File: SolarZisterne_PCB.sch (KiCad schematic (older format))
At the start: 4 parts

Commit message: Konzept auf I2C
Alle Temp und Strom Senoren werden über I2C angesteuert Digitale I/O werden auch über I2C erweiter. Kein AT MEGA mehr.
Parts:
- removed C? (x2): 22pF, symbol C
- removed U?: ATMEGA328P-PU, DIL28, symbol ATMEGA328P-PU
- removed Y?: Crystal 8MHz, symbol Crystal
- added JP?: Jumper_NO_Small, symbol Jumper_NO_Small
- added U?: WeMos_mini, symbol WeMos_mini
- added U?: MCP23008, symbol MCP23008
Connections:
- net labels removed: GND
- wire segments 15 -> 4
- no-connect marks 0 -> 4
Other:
- note added: "Pins D5, D6, D7, D8 werden durch SD Karte beansprucht\nPins D2, D1 werden für I2C Sensoren benutzt\nweitere 3 Pins für MCP73871 Solar Charger\nweitere 2 Pins für Ultraschallsensor"
- note added: "SDA\nSCL"
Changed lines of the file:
@@
 LIBS:contrib
 LIBS:valves
+LIBS:ESP8266
+LIBS:wemos_mini
+LIBS:SolarZisterne_PCB-cache
 EELAYER 25 0
 EELAYER END
@@
 $EndDescr
 $Comp
-L ATMEGA328P-PU U?
-U 1 1 5929E6B8
-P 3600 2600
-F 0 "U?" H 2850 3850 50  0000 L BNN
-F 1 "ATMEGA328P-PU" H 4000 1200 50  0000 L BNN
-F 2 "DIL28" H 3600 2600 50  0001 C CIN
-F 3 "" H 3600 2600 50  0001 C CNN
-	1    3600 2600
+L WeMos_mini U?
+U 1 1 59516611
+P 9250 1800
+F 0 "U?" H 9250 2300 60  0000 C CNN
+F 1 "WeMos_mini" H 9250 1300 60  0000 C CNN
+F 2 "" H 9800 1100 60  0000 C CNN
+F 3 "" H 9800 1100 60  0000 C CNN
+	1    9250 1800
 	1    0    0    -1
 $EndComp
+Text Notes 8250 950  0    60   ~ 0
+Pins D5, D6, D7, D8 werden durch SD Karte beansprucht\nPins D2, D1 werden für I2C Sensoren benutzt\nweitere 3 Pins für MCP73871 Solar Charger\nweitere 2 Pins für Ultraschallsensor
+NoConn ~ 9750 1850
+NoConn ~ 9750 1750
+NoConn ~ 9750 1650
+NoConn ~ 9750 1550
+Wire Wire Line
+	8750 1950 8050 1950
+Wire Wire Line
+	8750 1850 8050 1850
+Text Notes 7850 2000 0    60   ~ 0
+SDA\nSCL
 $Comp
-L GND #PWR?
-U 1 1 5929E77D
-P 2450 4000
-F 0 "#PWR?" H 2450 3750 50  0001 C CNN
-F 1 "GND" H 2450 3850 50  0000 C CNN
-F 2 "" H 2450 4000 50  0001 C CNN
-F 3 "" H 2450 4000 50  0001 C CNN
-	1    2450 4000
+L Jumper_NO_Small JP?
+U 1 1 59516939
+P 10000 2050
+F 0 "JP?" H 10000 2130 50  0000 C CNN
+F 1 "Jumper_NO_Small" H 10010 1990 50  0000 C CNN
+F 2 "" H 10000 2050 50  0001 C CNN
+F 3 "" H 10000 2050 50  0001 C CNN
+	1    10000 2050
+	0    1    1    0
+$EndComp
+Wire Wire Line
+	10000 2150 9750 2150
+Wire Wire Line
+	10000 1950 9750 1950
+$Comp
+L MCP23008 U?
+U 1 1 59516B77
+P 6750 2000
+F 0 "U?" H 6650 2625 50  0000 R CNN
+F 1 "MCP23008" H 6650 2550 50  0000 R CNN
+F 2 "" H 6800 1350 50  0001 L CNN
+F 3 "" H 7000 2600 50  0001 C CNN
+	1    6750 2000
 	1    0    0    -1
 $EndComp
-Wire Wire Line
-	2700 3800 2450 3800
-Wire Wire Line
-	2450 3700 2450 4000
-Wire Wire Line
-	2700 3700 2450 3700
-Connection ~ 2450 3800
-$Comp
-L Crystal Y?
-U 1 1 5929E800
-P 5000 2150
-F 0 "Y?" H 5000 2300 50  0000 C CNN
-F 1 "Crystal 8MHz" H 5000 2000 50  0000 C CNN
-F 2 "" H 5000 2150 50  0001 C CNN
-F 3 "" H 5000 2150 50  0001 C CNN
-	1    5000 2150
-	0    1    1    0
-$EndComp
-$Comp
-L C C?
-U 1 1 5929E857
-P 5300 2000
-F 0 "C?" H 5325 2100 50  0000 L CNN
-F 1 "22pF" H 5325 1900 50  0000 L CNN
-F 2 "" H 5338 1850 50  0001 C CNN
-F 3 "" H 5300 2000 50  0001 C CNN
-	1    5300 2000
-	0    -1   -1   0
-$EndComp
-$Comp
-L C C?
-U 1 1 5929E893
-P 5300 2300
-F 0 "C?" H 5325 2400 50  0000 L CNN
-F 1 "22pF" H 5325 2200 50  0000 L CNN
-F 2 "" H 5338 2150 50  0001 C CNN
-F 3 "" H 5300 2300 50  0001 C CNN
-	1    5300 2300
-	0    -1   -1   0
-$EndComp
-Wire Wire Line
-	4750 2000 5150 2000
-Wire Wire Line
-	4750 2300 5150 2300
-Wire Wire Line
-	4750 2000 4750 2100
-Wire Wire Line
-	4750 2100 4600 2100
-Connection ~ 5000 2000
-Wire Wire Line
-	4750 2300 4750 2200
-Wire Wire Line
-	4750 2200 4600 2200
-Connection ~ 5000 2300
-$Comp
-L GND #PWR?
-U 1 1 5929EA3D
-P 5600 2400
-F 0 "#PWR?" H 5600 2150 50  0001 C CNN
-F 1 "GND" H 5600 2250 50  0000 C CNN
-F 2 "" H 5600 2400 50  0001 C CNN
-F 3 "" H 5600 2400 50  0001 C CNN
-	1    5600 2400
-	1    0    0    -1
-$EndComp
-Wire Wire Line
-	5450 2300 5600 2300
-Wire Wire Line
-	5600 2000 5600 2400
-Wire Wire Line
-	5450 2000 5600 2000
-Connection ~ 5600 2300
-$Comp
-L GND #PWR?
-U 1 1 5929EA91
-P 2450 2200
-F 0 "#PWR?" H 2450 1950 50  0001 C CNN
-F 1 "GND" H 2450 2050 50  0000 C CNN
-F 2 "" H 2450 2200 50  0001 C CNN
-F 3 "" H 2450 2200 50  0001 C CNN
-	1    2450 2200
-	1    0    0    -1
-$EndComp
-Wire Wire Line
-	2700 2100 2450 2100
-Wire Wire Line
-	2450 1800 2450 2200
-Wire Wire Line
-	2700 1800 2450 1800
-Connection ~ 2450 2100
 $EndSCHEMATC

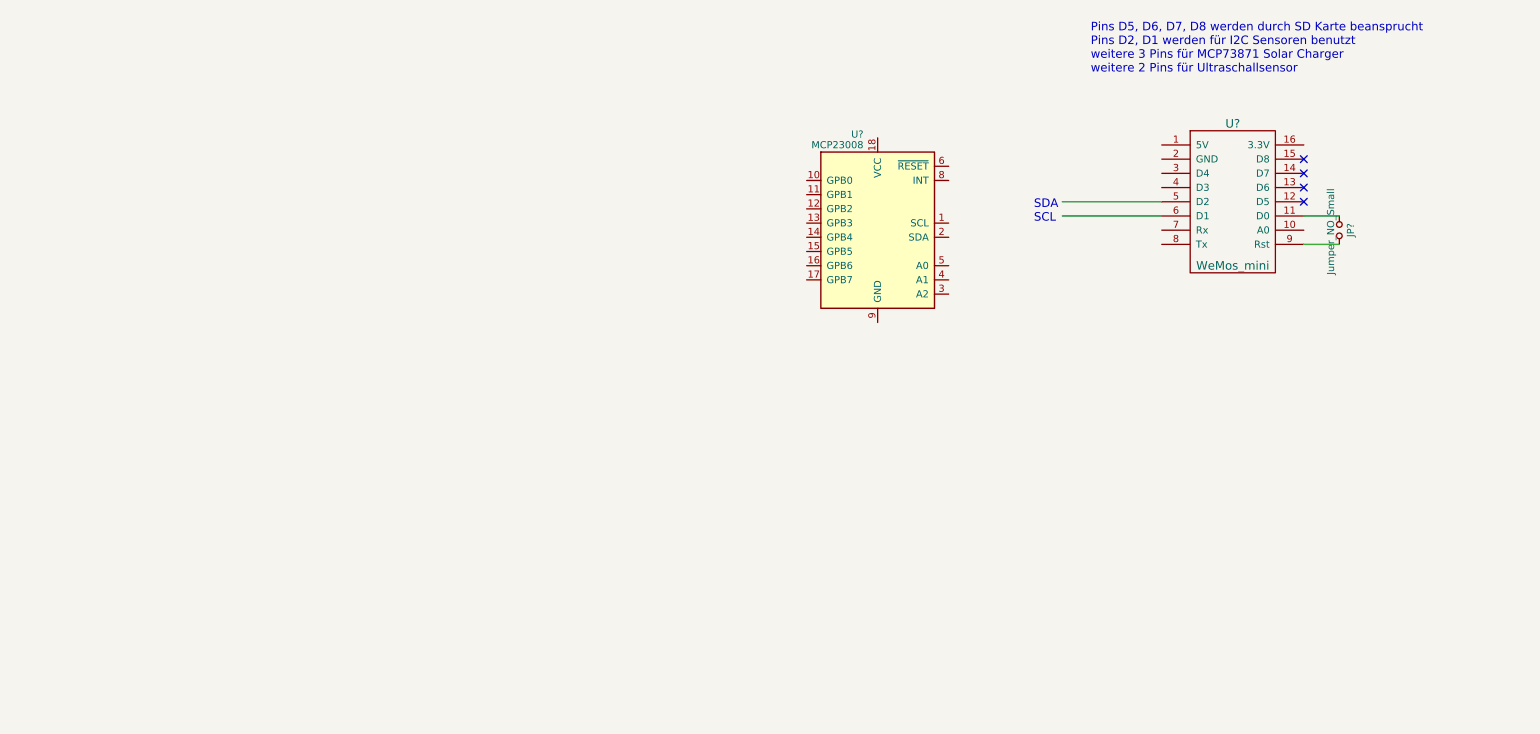
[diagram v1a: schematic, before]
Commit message: Erster Entwurf des kompletten Schaltplans
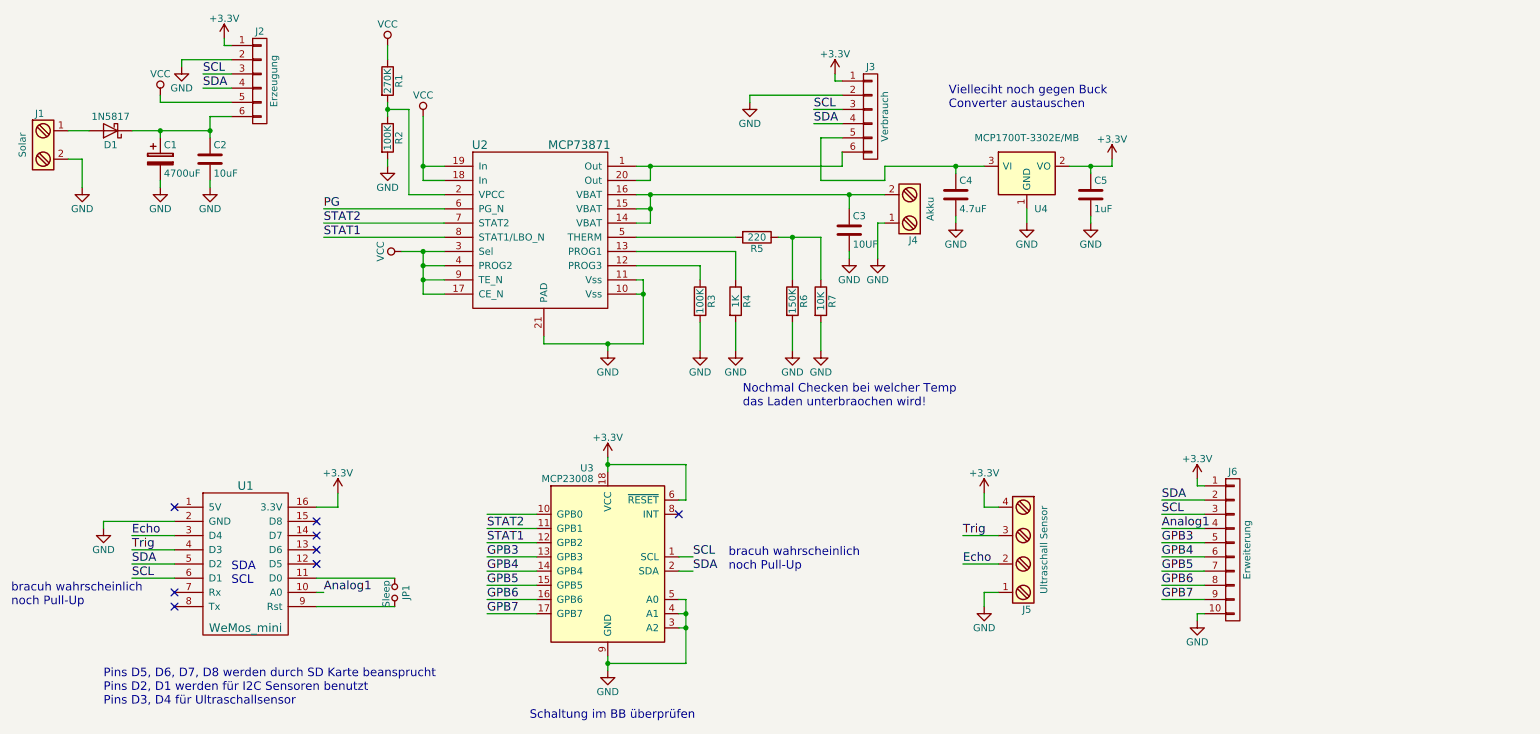
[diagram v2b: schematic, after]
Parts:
- added C1: 4700uF, symbol CP
- added C2: 10uF, symbol C
- added C3: 10UF, symbol C
- added C4: 4.7uF, symbol C
- added C5: 1uF, symbol C
- added D1: 1N5817, symbol D_Schottky
- added J1: Solar, symbol Screw_Terminal_1x02
- added J2: Erzeugung, symbol CONN_01X06
- added J3: Verbrauch, symbol CONN_01X06
- added J4: Akku, symbol Screw_Terminal_1x02
- added J5: Ultraschall Sensor, symbol Screw_Terminal_1x04
- added J6: Erweiterung, symbol CONN_01X10
- added R1: 270K, symbol R
- added R2, R3: 100K, symbol R
- added R4: 1K, symbol R
- added R5: 220, symbol R
- added R6: 150K, symbol R
- added R7: 10K, symbol R
- added U2: MCP73871, symbol MCP73871
- added U4: MCP1700T-3302E/MB, symbol MCP1700T-3002E/TT
- JP1: renamed from JP?; value Jumper_NO_Small -> Sleep
- gave numbers to parts that had none: 2
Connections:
- net labels added: +3.3V, Analog1, Echo, GND, GPB3, GPB4, GPB5, GPB6, GPB7, PG, SCL, SDA, STAT1, STAT2, Trig, VCC
- wire segments 4 -> 131
- no-connect marks 4 -> 8
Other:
- note added: "Nochmal Checken bei welcher Temp\ndas Laden unterbraochen wird!\n"
- note added: "Pins D5, D6, D7, D8 werden durch SD Karte beansprucht\nPins D2, D1 werden für I2C Sensoren benutzt\nPins D3, D4 für Ultraschallsensor"
- note added: "Schaltung im BB überprüfen"
- note added: "Vielleciht noch gegen Buck \nConverter austauschen"
- note added: "bracuh wahrscheinlich\nnoch Pull-Up"
- note removed: "Pins D5, D6, D7, D8 werden durch SD Karte beansprucht\nPins D2, D1 werden für I2C Sensoren benutzt\nweitere 3 Pins für MCP73871 Solar Charger\nweitere 2 Pins für Ultraschallsensor"
- moved on the sheet: JP1, U1, U3

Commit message: Thermal Sensoren eingefügt
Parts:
- added J7: Externer Temperatur Sensor, symbol Screw_Terminal_1x04
- added J8: Externer Temperatur Sensor, symbol CONN_01X04
- R1, R2, R3, R4, R5, R6, R7: footprint (none) -> Resistors_THT:R_Axial_DIN0207_L6.3mm_D2.5mm_P10.16mm_Horizontal
- U1: footprint (none) -> wemos_d1_mini:D1_mini_board
- U2: footprint (none) -> Housings_DIP:DIP-18_W7.62mm_LongPads
- U3: footprint (none) -> Housings_DFN_QFN:QFN-20-1EP_4x4mm_Pitch0.5mm
- U4: footprint (none) -> TO_SOT_Packages_THT:TO-92_Inline_Narrow_Oval
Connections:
- net +3V3: now also J7.4, J8.1 (P1)
- net GND: now also J7.3, J8.2 (P2)
- net PG: now also U3.10 (GPB0)
- net SCL: now also J7.2, J8.3 (P3)
- net SDA: now also J7.1, J8.4 (P4)
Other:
- moved on the sheet: J5, J6

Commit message: PCB angefangen
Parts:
- C1: footprint (none) -> Capacitors_THT:CP_Radial_D16.0mm_P7.50mm
- C2: footprint (none) -> Capacitors_THT:C_Disc_D5.0mm_W2.5mm_P2.50mm
- C3: renamed from C4; footprint (none) -> Capacitors_THT:C_Disc_D5.0mm_W2.5mm_P2.50mm
- C4: renamed from C5; footprint (none) -> Capacitors_THT:C_Disc_D5.0mm_W2.5mm_P2.50mm
- C5: renamed from C3; value 10UF -> 10uF; footprint (none) -> Capacitors_THT:C_Disc_D5.0mm_W2.5mm_P2.50mm
- D1: footprint (none) -> Diodes_THT:D_DO-41_SOD81_P10.16mm_Horizontal
- J1: renamed from J2; footprint (none) -> Pin_Headers:Pin_Header_Straight_1x06_Pitch2.54mm; symbol CONN_01X06 -> CONN_01X06-RESCUE-SolarZisterne_PCB
- J2: renamed from J3; footprint (none) -> Pin_Headers:Pin_Header_Straight_1x06_Pitch2.54mm; symbol CONN_01X06 -> CONN_01X06-RESCUE-SolarZisterne_PCB
- J3: renamed from J1; footprint (none) -> Connectors_Terminal_Blocks:TerminalBlock_Pheonix_MKDS1.5-2pol
- J4: footprint (none) -> Connectors_Terminal_Blocks:TerminalBlock_Pheonix_MKDS1.5-2pol
- J5: footprint (none) -> Connectors_Terminal_Blocks:TerminalBlock_Pheonix_MKDS1.5-4pol
- J6: renamed from J7; footprint (none) -> Connectors_Terminal_Blocks:TerminalBlock_Pheonix_MKDS1.5-4pol
- J7: renamed from J8; value Externer Temperatur Sensor -> Interner Temperatur Sensor; footprint (none) -> Pin_Headers:Pin_Header_Straight_1x04_Pitch2.54mm
- J8: renamed from J6; footprint (none) -> Pin_Headers:Pin_Header_Straight_1x10_Pitch2.54mm
- JP1: footprint (none) -> Pin_Headers:Pin_Header_Straight_1x02_Pitch2.54mm
- U3: renamed from U1; symbol WeMos_mini -> WeMos_mini-RESCUE-SolarZisterne_PCB
- renumbered R5 to R3, R3 to R4, R4 to R5, U4 to U1, U3 to U4

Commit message: weiter gearbeite
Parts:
- U2: footprint Housings_DIP:DIP-18_W7.62mm_LongPads -> Housings_DFN_QFN:QFN-20-1EP_4x4mm_Pitch0.5mm
- U4: footprint Housings_DFN_QFN:QFN-20-1EP_4x4mm_Pitch0.5mm -> Housings_DIP:DIP-18_W7.62mm_LongPads
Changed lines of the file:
@@
 F 0 "U4" H 4750 4975 50  0000 R CNN
 F 1 "MCP23008" H 4750 4900 50  0000 R CNN
-F 2 "Housings_DFN_QFN:QFN-20-1EP_4x4mm_Pitch0.5mm" H 4900 3700 50  0001 L CNN
+F 2 "Housings_DIP:DIP-18_W7.62mm_LongPads" H 4900 3700 50  0001 L CNN
 F 3 "" H 5100 4950 50  0001 C CNN
 	1    4850 4350
@@
 F 0 "U2" H 3950 3050 60  0000 C CNN
 F 1 "MCP73871" H 4650 3050 60  0000 C CNN
-F 2 "Housings_DIP:DIP-18_W7.62mm_LongPads" H 4150 2300 60  0001 C CNN
+F 2 "Housings_DFN_QFN:QFN-20-1EP_4x4mm_Pitch0.5mm" H 4150 2300 60  0001 C CNN
 F 3 "" H 4150 2300 60  0000 C CNN
 	1    4400 2250
@@
 L +3.3V #PWR032
 U 1 1 5956BC5D
-P 8150 3850
-F 0 "#PWR032" H 8150 3700 50  0001 C CNN
-F 1 "+3.3V" H 8150 3990 50  0000 C CNN
-F 2 "" H 8150 3850 50  0001 C CNN
-F 3 "" H 8150 3850 50  0001 C CNN
-	1    8150 3850
+P 8150 3900
+F 0 "#PWR032" H 8150 3750 50  0001 C CNN
+F 1 "+3.3V" H 8150 4040 50  0000 C CNN
+F 2 "" H 8150 3900 50  0001 C CNN
+F 3 "" H 8150 3900 50  0001 C CNN
+	1    8150 3900
 	1    0    0    -1
 $EndComp
@@
 	8250 4000 8150 4000
 Wire Wire Line
-	8150 4000 8150 3850
+	8150 4000 8150 3900
 Wire Wire Line
 	8250 4400 8000 4400
